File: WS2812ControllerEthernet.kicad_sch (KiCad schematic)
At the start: 9 parts, among them J1 Conn_01x04_Male, J2 Conn_01x03_Male, J3 Conn_01x04_Male, J4 Conn_01x02_Male, U1 WT32_ETH01, U2 SN74AHCT125

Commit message: Updated layout
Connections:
- net GND: now also U1.17 (GND), U1.2 (GND), U1.26 (GND), U1.9 (GND)
- no-connect marks 26 -> 22

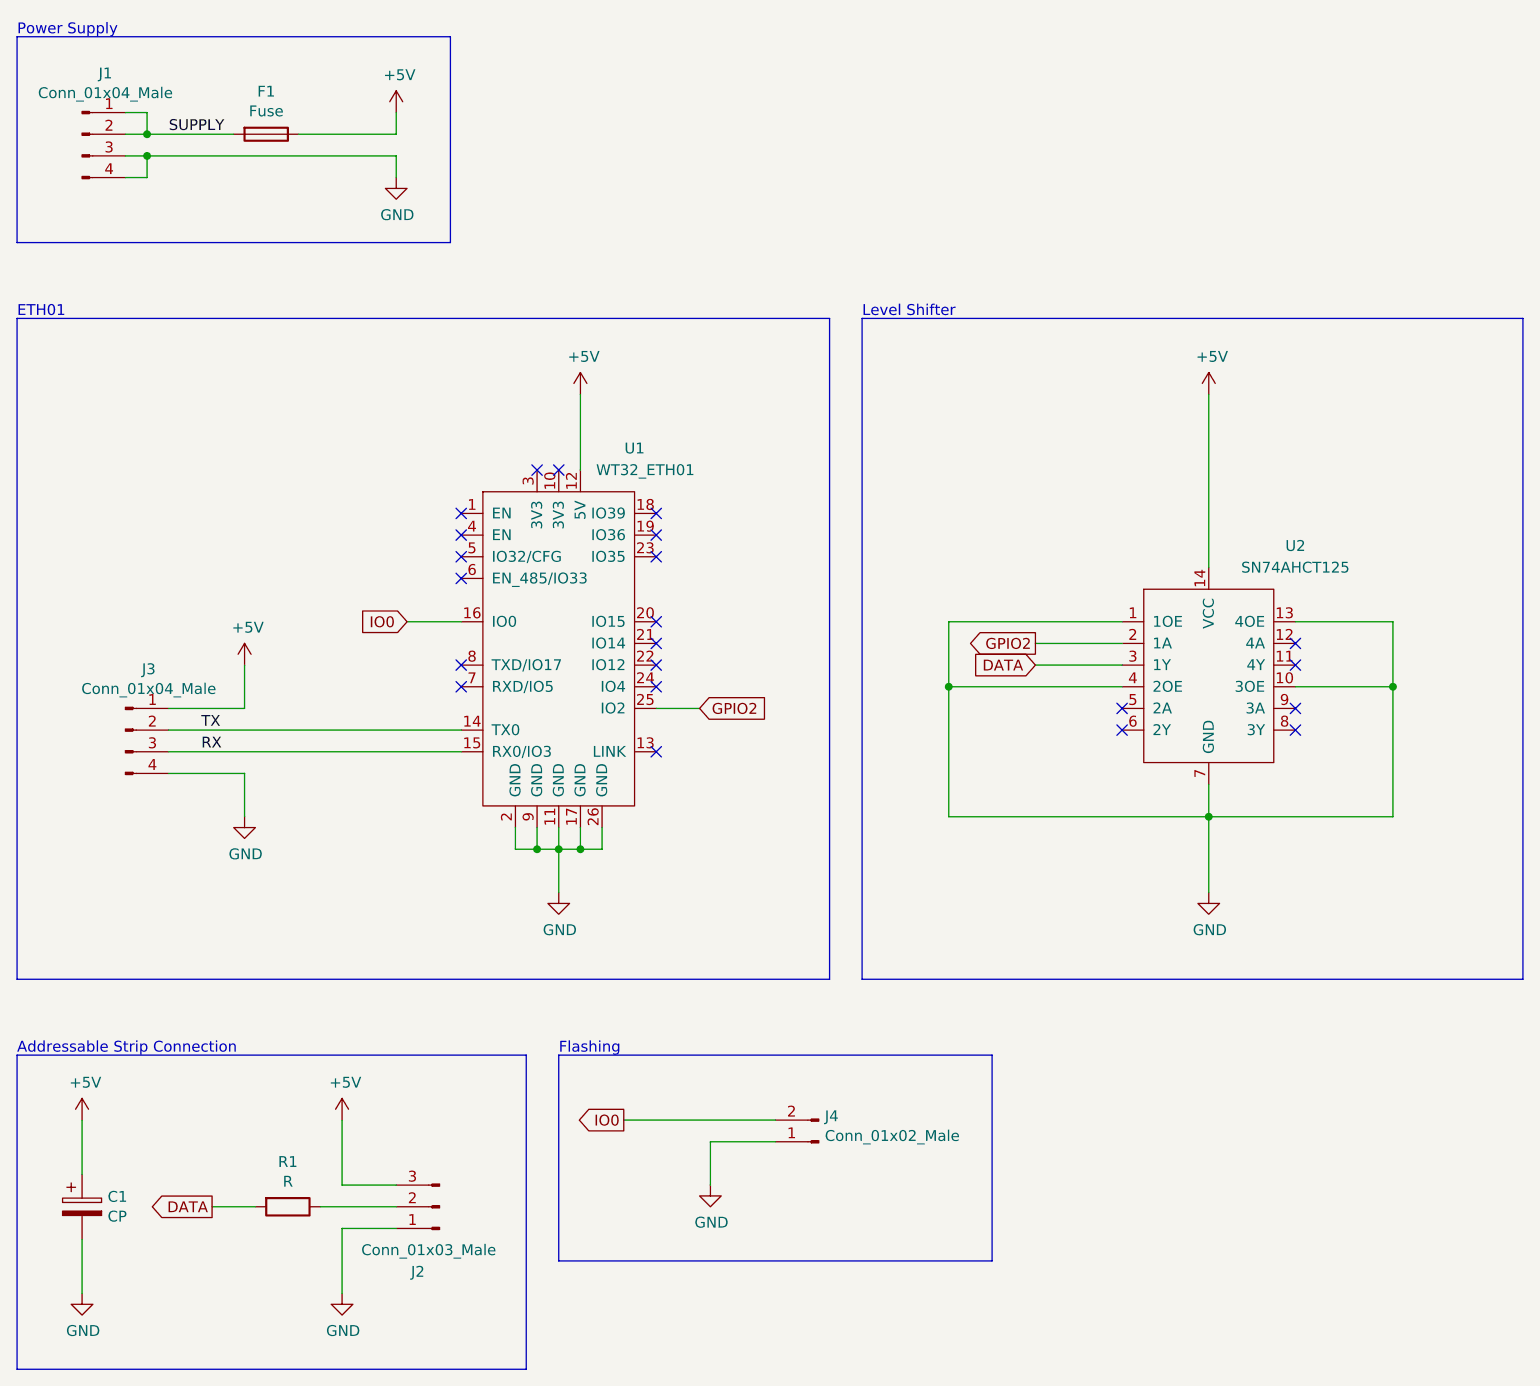
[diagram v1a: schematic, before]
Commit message: Added additional GPIO for strip
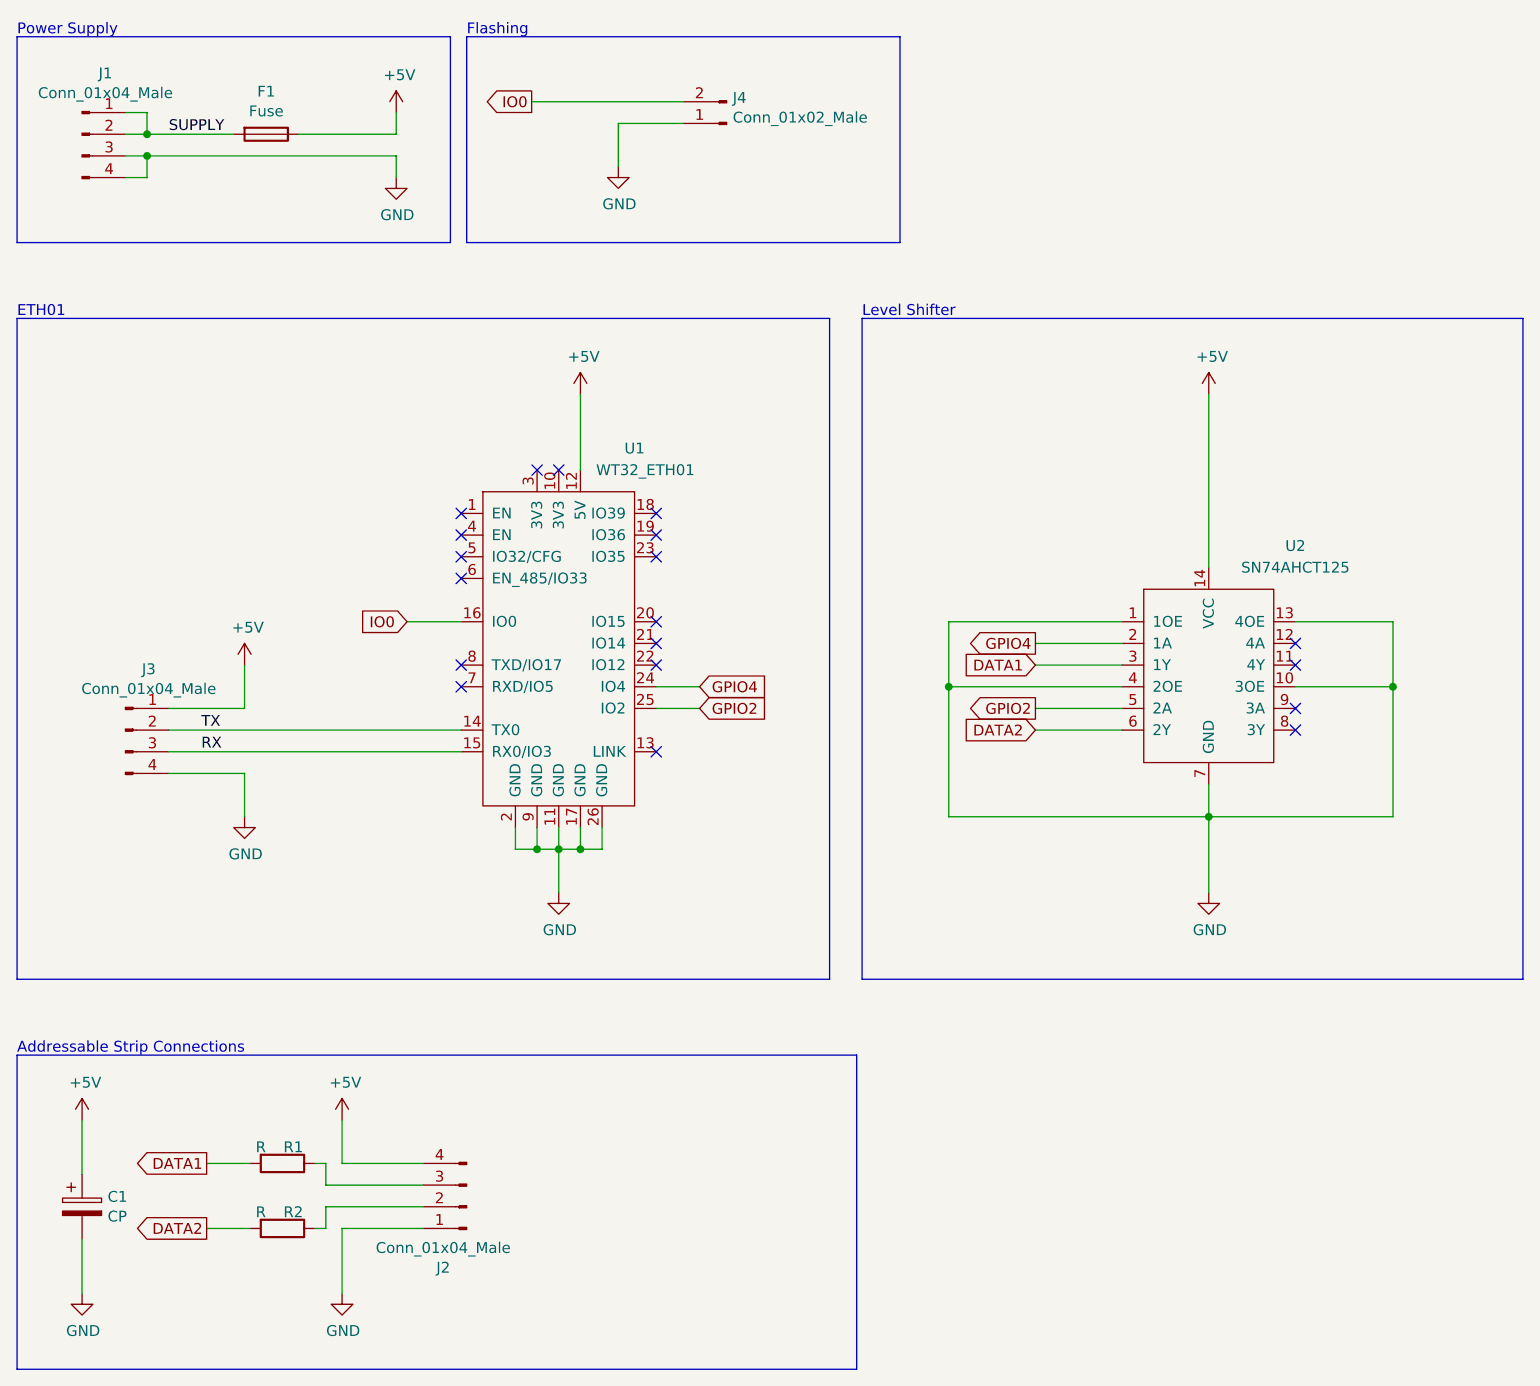
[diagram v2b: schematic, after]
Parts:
- removed J2: Conn_01x03_Male, TerminalBlock_Phoenix:TerminalBlock_Phoenix_MPT-0,5-3-2.54_1x03_P2.54mm_Horizontal, symbol Connector:Conn_01x03_Male
- added J2: Conn_01x04_Male, TerminalBlock_Phoenix:TerminalBlock_Phoenix_MPT-0,5-4-2.54_1x04_P2.54mm_Horizontal, symbol Connector:Conn_01x04_Male
- added R2: R, Resistor_SMD:R_0805_2012Metric_Pad1.20x1.40mm_HandSolder, symbol Device:R
- F1: footprint halibs:Fuse-PTF75_Stelvio -> haus-automatisierung:Fuse-PTF75_Stelvio
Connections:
- net +5V: now also J2.4 (Pin_4)
- net GND: now also J2.1 (Pin_1)
- net GPIO2: now also U2.5 (2A); no longer U2.2 (1A)
- net GPIO4: now reaches U1.24 (IO4)
- net GPIO4: now also U2.2 (1A)
- net at R1.1: now also J2.3 (Pin_3)
- net DATA2: now reaches U2.6 (2Y)
- net DATA2: now also R2.2
- net DATA renamed DATA1
- new net: J2.2 (Pin_2), R2.1
- no-connect marks 22 -> 19
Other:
- note added: "Addressable Strip Connections"
- note removed: "Addressable Strip Connection"
- moved on the sheet: J4, R1

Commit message: KiCad 8
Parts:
- removed J1, J2: Conn_01x04_Male, TerminalBlock_Phoenix:TerminalBlock_Phoenix_MPT-0,5-4-2.54_1x04_P2.54mm_Horizontal, symbol Connector:Conn_01x04_Male
- added J1: Barrel_Jack_MountingPin, Connector_BarrelJack:BarrelJack_Wuerth_6941xx301002, symbol Connector:Barrel_Jack_MountingPin
- added J2, J3: Conn_01x03_Pin, TerminalBlock_Phoenix:TerminalBlock_Phoenix_MPT-0,5-3-2.54_1x03_P2.54mm_Horizontal, symbol Connector:Conn_01x03_Pin
- renumbered J3 to J4, J4 to J5
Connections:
- net +5V: now also J2.3 (Pin_3), J3.3 (Pin_3)
- net GND: now also J1.2, J2.1 (Pin_1), J3.1 (Pin_1)
- net SUPPLY: now also J1.1
- net D4: now reaches R1.1
- net D4: now also J2.2 (Pin_2)
- net D2: now reaches R2.1
- net D2: now also J3.2 (Pin_2)
- no-connect marks 19 -> 20
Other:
- moved on the sheet: F1, J5, R1, R2

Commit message: v2.0
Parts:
- U1: footprint haus-automatisierung:WT32_ETH01 -> haus-automatisierung:WT32_ETH01_long
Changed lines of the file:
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@@
 	(title_block
 		(title "WS2812-Controller Ethernet")
-		(date "2024-05-24")
-		(rev "1.1")
+		(date "2024-08-23")
+		(rev "2.0")
 		(company "haus-automatisierung.com")
 		(comment 1 "Matthias Kleine")
@@
 			)
 		)
-		(property "Footprint" "haus-automatisierung:WT32_ETH01"
+		(property "Footprint" "haus-automatisierung:WT32_ETH01_long"
 			(at 99.06 68.58 0)
 			(effects
